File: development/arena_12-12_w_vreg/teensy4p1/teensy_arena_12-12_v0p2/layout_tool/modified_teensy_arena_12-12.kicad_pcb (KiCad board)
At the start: 4 copper layers, 228.6 x 228.6 mm, 123 parts, among them J1 Barrel_Jack, J2 Conn_01x04, J3 Conn_01x04, P1 CONN15, P10 CONN15, P11 CONN15, P12 CONN15, P2 CONN15, P3 CONN15, P4 CONN15, P5 CONN15, P6 CONN15, P7 CONN15, P8 CONN15, P9 CONN15, Q2 MOSFET_NCHAN, SW1 SW_SPDT, U1 TXB0108PW, U10 TPS564201DDC, U11 TPS564201DDC, U12 TPS564201DDC, U13 TPS564201DDC, U14 TPS564201DDC, U15 TPS564201DDC, U16 TPS564201DDC, U17 TPS564201DDC, U18 Teensy4.1, U2 TXB0108PW, U3 TXB0108PW, U4 TXB0108PW, U5 TXB0108PW, U6 TPS564201DDC, U7 TPS564201DDC, U8 TPS564201DDC, U9 TPS564201DDC

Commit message: Worked on teensy41 arena w/ vreg.
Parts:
- moved J2 43.4 mm to (288.7, 185.8)
- moved J3 43.4 mm to (288.7, 176.8)
- moved C1 34.7 mm to (288.1, 209.6)
- moved C2 34.7 mm to (288.2, 223.0)
- moved U1 34.7 mm to (285.8, 216.6)
- moved R1 22.1 mm to (288.5, 132.9)
- moved Q2 22.1 mm to (286.5, 129.6)
- moved R2 22.1 mm to (290.4, 129.6)
- moved C10 6.25 mm to (106.7, 285.7)
- moved C5 6.25 mm to (214.2, 286.3)
- moved C6 6.25 mm to (201.9, 286.3)
- moved C7 6.25 mm to (166.6, 286.5)
- moved C8 6.25 mm to (154.2, 286.5)
- moved C9 6.25 mm to (118.9, 285.8)
- moved U3 6.25 mm to (208.1, 284.1)
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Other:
- outline, holes or cut-outs redrawn

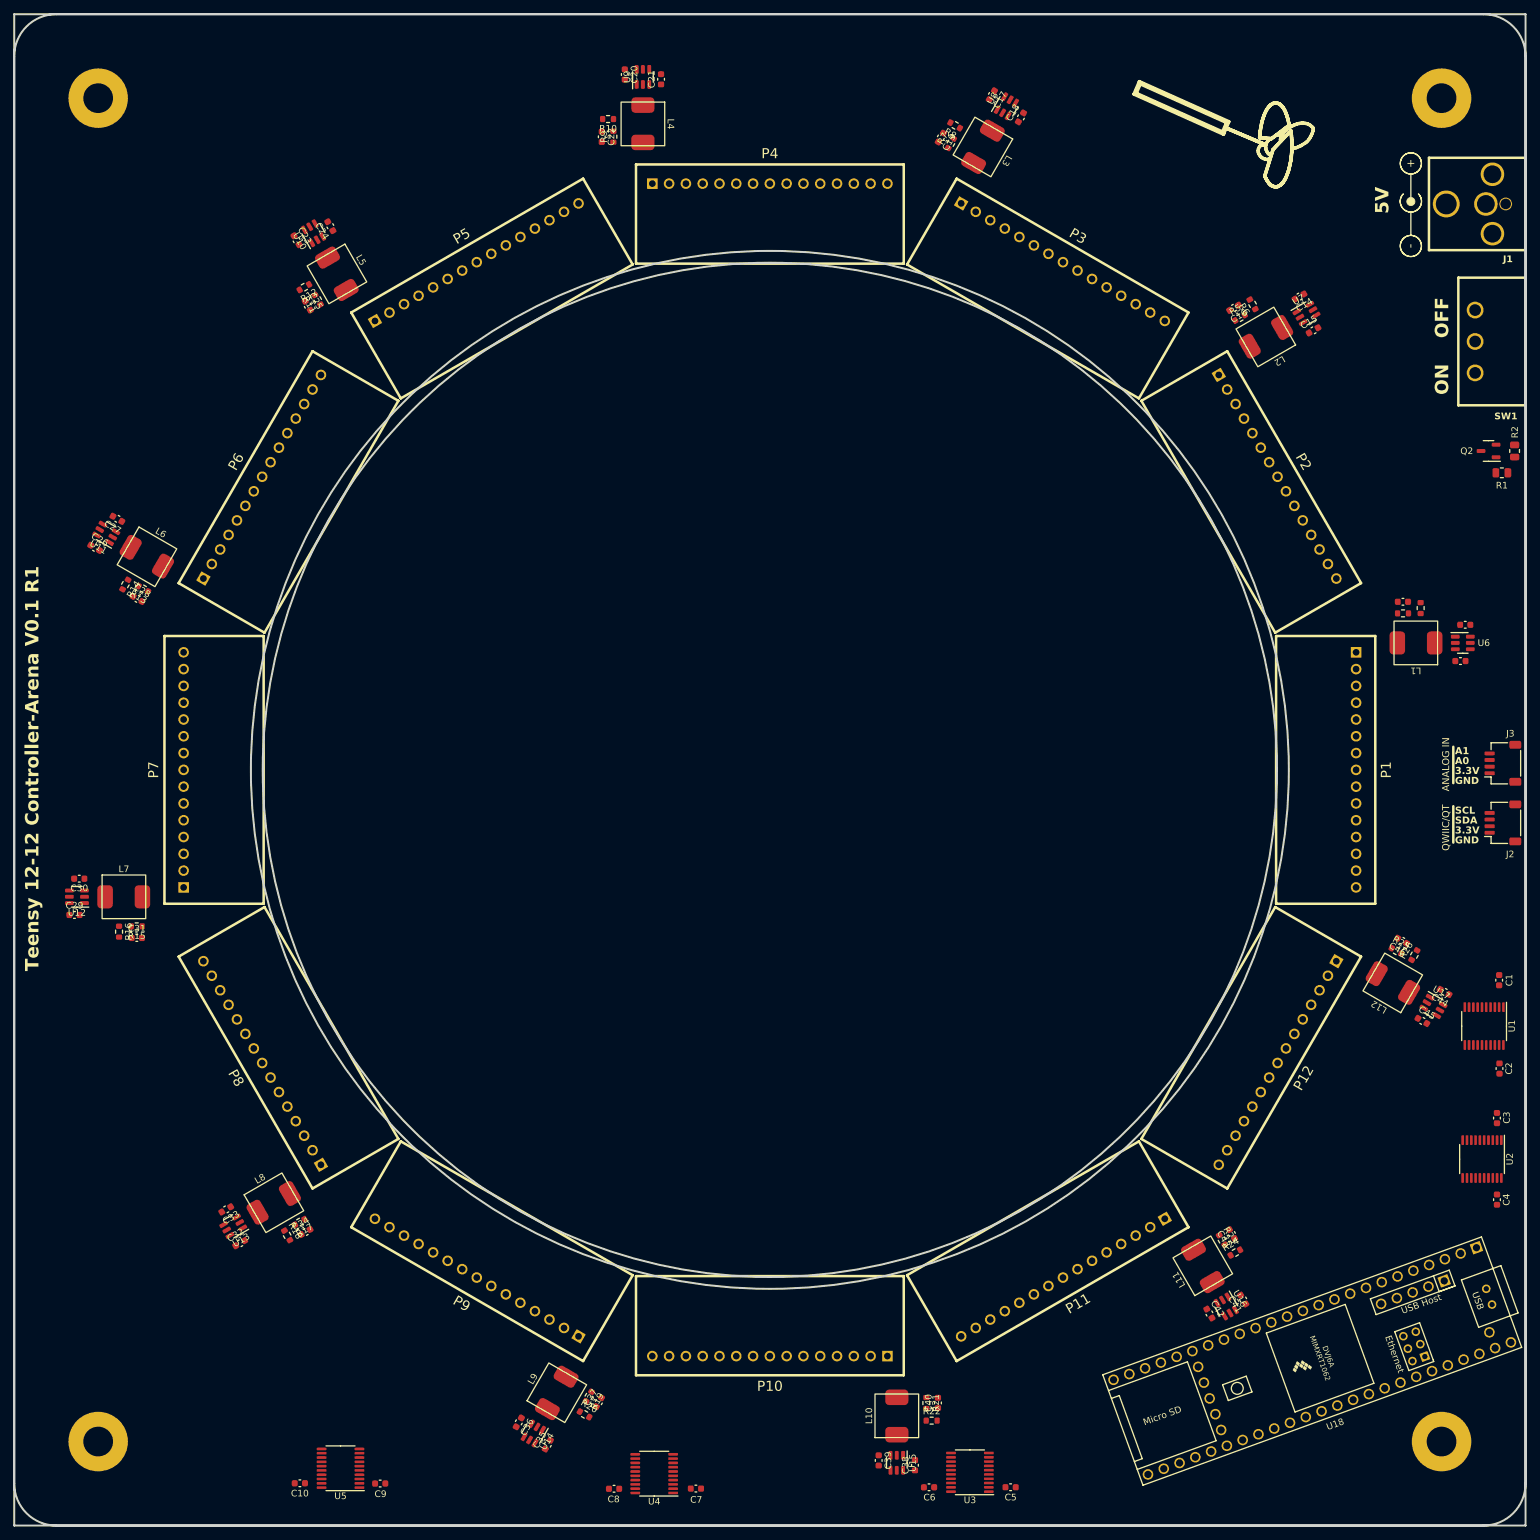
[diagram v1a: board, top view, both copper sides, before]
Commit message: Worked on routing for teensy vreg arena.
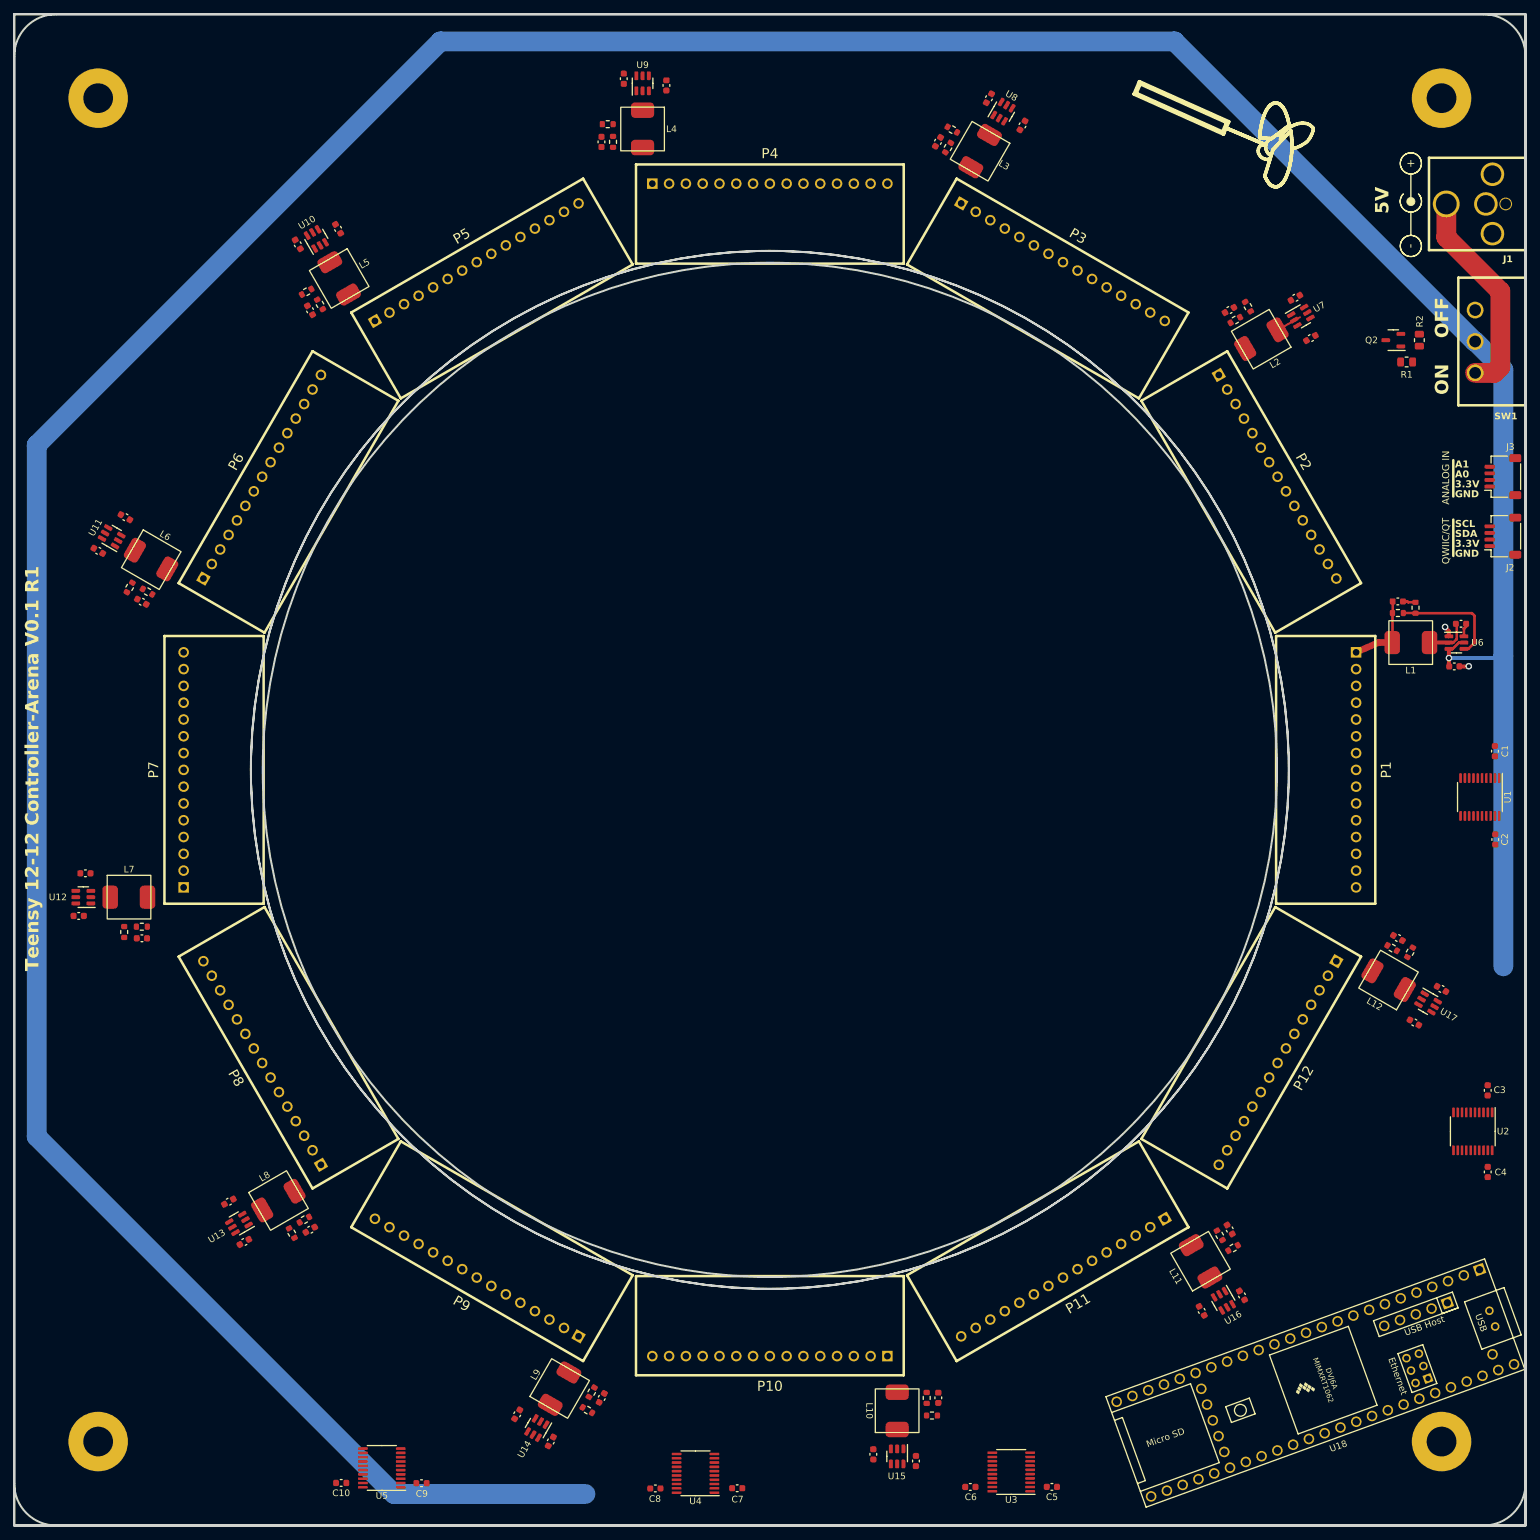
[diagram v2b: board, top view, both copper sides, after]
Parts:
- C11: value 100nF -> 10uF
- C12: value 10uF -> 100nF
- moved J2 43.4 mm to (288.7, 142.5)
- moved J3 43.4 mm to (288.7, 133.5)
- moved C1 34.7 mm to (287.5, 175.0)
- moved C2 34.7 mm to (287.5, 188.3)
- moved U1 34.7 mm to (285.2, 181.9)
- moved R1 22.1 mm to (274.1, 116.1)
- moved Q2 22.1 mm to (272.1, 112.8)
- moved R2 22.1 mm to (276.0, 112.8)
- moved C38 6.51 mm to (193.4, 281.3), turned to -90 degrees
- moved C11 6.51 mm to (281.3, 162.2), turned to 0 degrees
- moved C20 6.51 mm to (162.2, 74.3), turned to 90 degrees
- moved C29 6.51 mm to (74.3, 193.4), turned to 180 degrees
- moved C23 6.51 mm to (112.5, 96.0), turned to 120 degrees
- moved C32 6.51 mm to (96.0, 243.1), turned to -150 degrees
- moved C14 6.51 mm to (259.6, 112.5), turned to 30 degrees
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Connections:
- net Net-(SW1-A) renamed /Power & Voltage Regulators/SW_VCC
- C11 pad 1: Net-(U6-VBST) -> VCC
- C11 pad 2: Net-(U6-SW) -> GND
- C12 pad 1: VCC -> Net-(U6-VBST)
- C12 pad 2: GND -> Net-(U6-SW)
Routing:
- net VCC: track 0.00 -> 581.6 mm, vias 0 -> 1
- net /Power & Voltage Regulators/SW_VCC: track 0.00 -> 33.0 mm
- net Net-(U6-VFB): track 0.00 -> 17.0 mm
- net /Panel Headers/POW.5V_HDR_1: track 0.00 -> 12.0 mm
- net Net-(U6-SW): track 0.00 -> 6.69 mm
- net GND: track 0.00 -> 5.22 mm, vias 0 -> 2
- net Net-(U7-SW): track 0.00 -> 3.12 mm
- net Net-(U6-VBST): track 0.00 -> 2.04 mm
- added copper zone on In1.Cu, net (none)
- added copper zone on In2.Cu, net GND
